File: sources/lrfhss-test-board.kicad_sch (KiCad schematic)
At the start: 9 parts, among them J1 USB-C, U1 LoRa126XF30

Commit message: feat: add initial version of the schematic
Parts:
- added C1, C2: 1uF, footprints:CAP0805, symbol capacitors:C0805C105K5RACTU
- added C3: 47uF, footprints:CAP2917POL, symbol capacitors:T495X476K035ATE300
- added C4: 100nF, footprints:CAP0603, symbol capacitors:C0603C104K5RACTU
- added D1: LED, symbol Device:LED
- added J2, J3: 532610271, footprints:532610271, symbol 532610271:532610271
- added J4: 532610471, footprints:532610471, symbol 532610471:532610471
- added R4: 1k, footprints:RES0603, symbol resistors:CRCW06031K00FKEAHP
- added U2: AMS1117-3.3, Package_TO_SOT_SMD:SOT-223-3_TabPin2, symbol Regulator_Linear:AMS1117-3.3
- J1: footprint (none) -> footprinst:GENERIC-USB-C.step
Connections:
- net GND: now also J1.A1 (GND), J1.B1 (GND), U1.15 (GND), U1.2 (GND), U1.8 (GND), C1.1, C2.1, C3.2, C4.1, D1.1 (K), U2.1 (GND)
- net VBUS: now also J1.A4 (VBUS), J1.B4 (VBUS), U1.1 (VCC), C1.2, C3.1, C4.2, R4.2, U2.3 (VI)
- net SPI1: now reaches U1.10 (MISO)
- net SPI1: now also J4.2
- net SPI0: now reaches U1.11 (MOSI)
- net SPI0: now also J4.1
- net DATA1: now reaches U1.13 (DIO1)
- net DATA1: now also J3.2
- net DATA0: now reaches U1.14 (DIO3)
- net DATA0: now also J3.1
- net ANT: now reaches U1.16 (ANT)
- net CTRL0: now reaches U1.5 (~{RESET})
- net CTRL0: now also J2.1
- net CTRL1: now reaches U1.6 (BUSY)
- net CTRL1: now also J2.2
- net SPI3: now reaches U1.7 (~{NSS})
- net SPI3: now also J4.4
- net SPI2: now reaches U1.9 (SCK)
- net SPI2: now also J4.3
- new net: D1.2 (A), R4.1
- new net 3V3: C2.2, U2.2 (VO)
- no-connect marks 0 -> 6
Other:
- moved on the sheet: R1, R2, R3, U1

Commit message: feat: improve schematic and layout
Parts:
- added J5: 142-0701-801, footprints:142-0701-801, symbol connectors:142-0701-801
- D1: footprint (none) -> LED_SMD:LED_0603_1608Metric
- J1: footprint footprinst:GENERIC-USB-C.step -> footprints:GENERIC-USB-C
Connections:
- net ANT: now also J5.1
- net CTRL0: now also J2.2; no longer J2.1
- net CTRL1: now also J2.1; no longer J2.2
- net GND: now also J5.S1, J5.S2, J5.S3, J5.S4
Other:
- moved on the sheet: C1, C2, C3, C4, D1, J1, J2, J3, J4, R1, R2, R3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

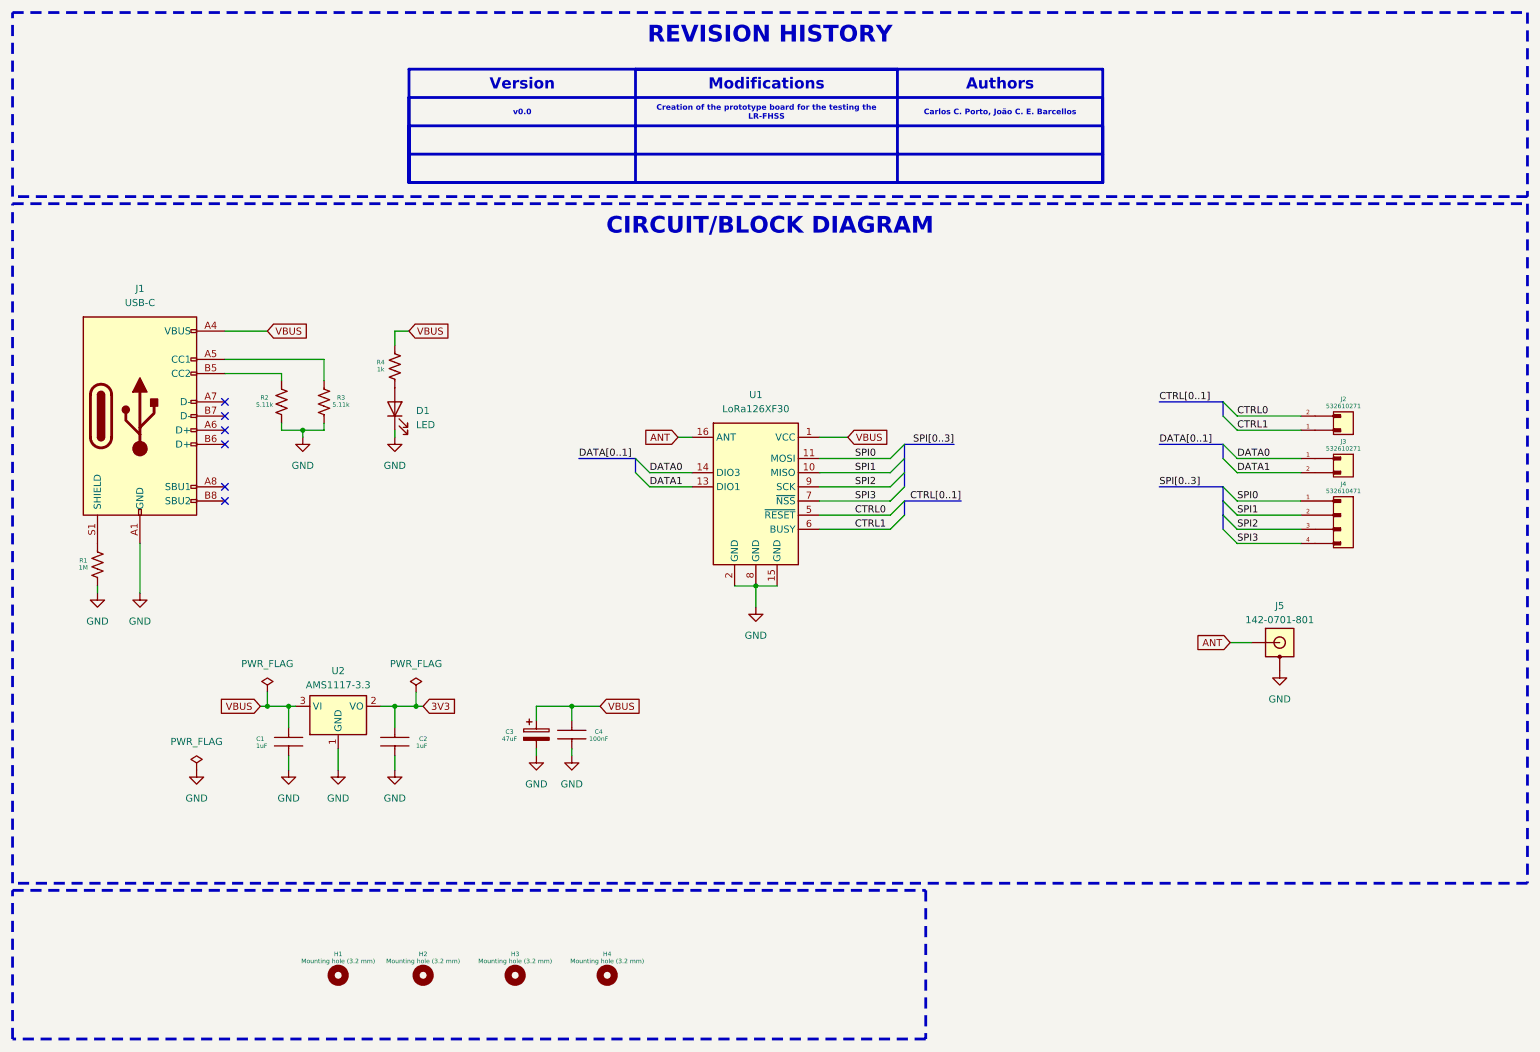
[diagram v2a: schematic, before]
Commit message: fix: add pins to interface with jumpers and some connectors for power
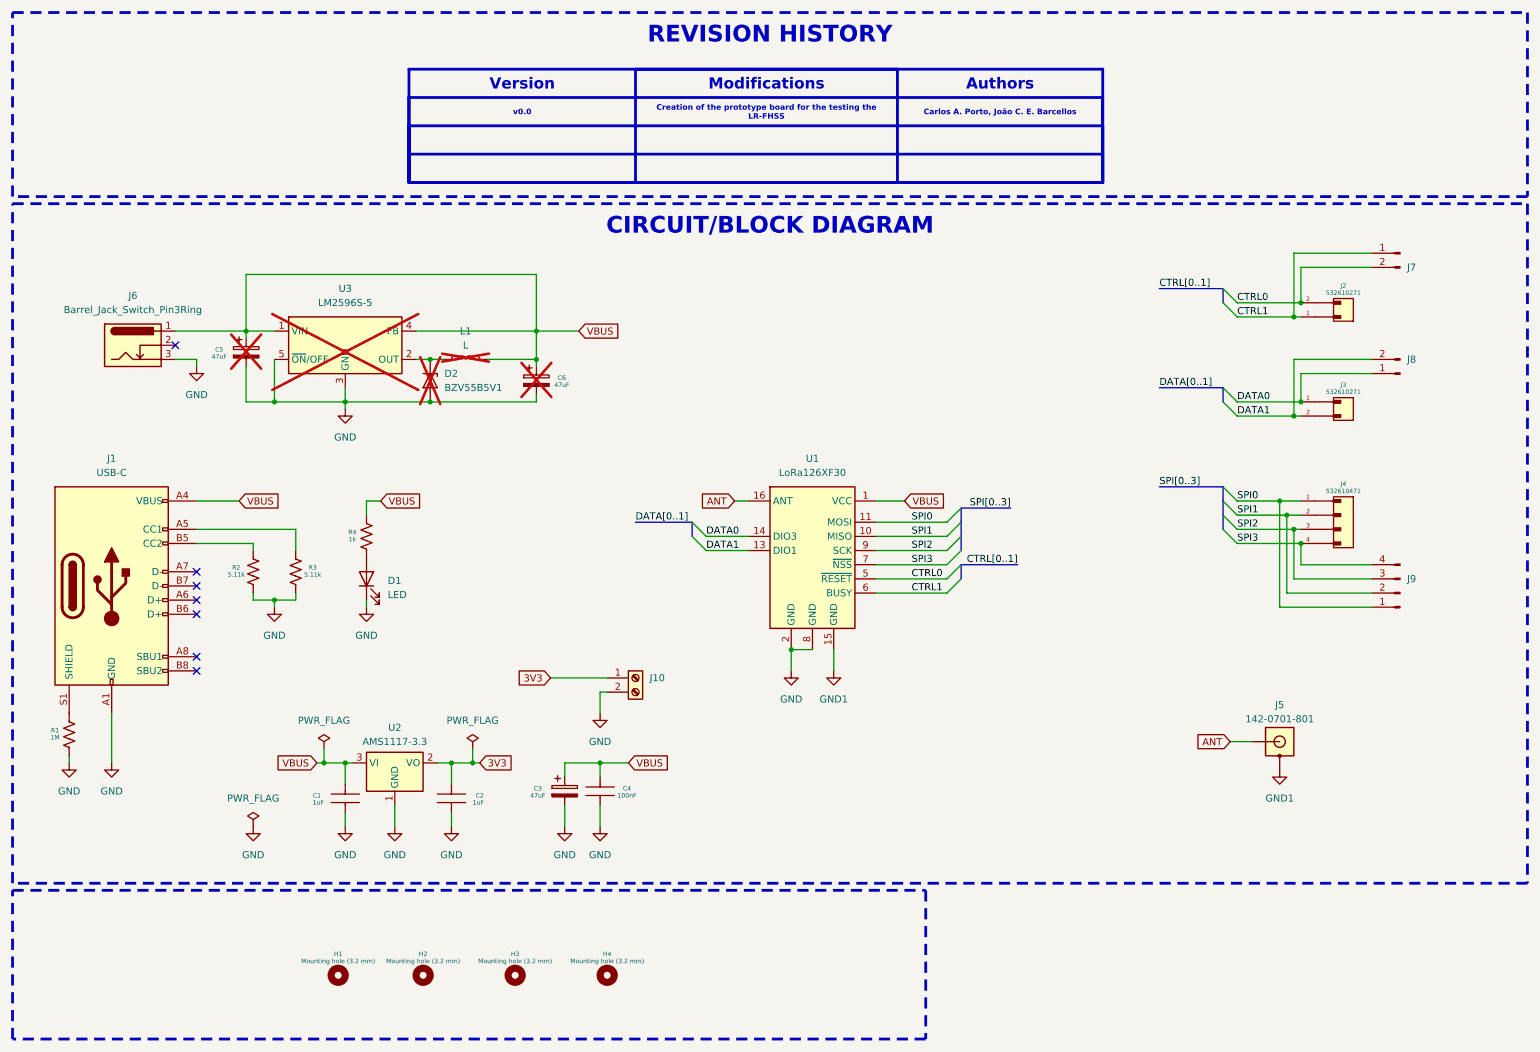
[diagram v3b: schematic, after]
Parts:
- added C5, C6: 47uF, footprints:CAP2917POL, symbol capacitors:T495X476K035ATE300
- added D2: BZV55B5V1, Diode_SMD:D_MiniMELF, symbol Diode:BZV55B5V1
- added J10: Screw_Terminal_01x02, footprints:MV-152, symbol Connector:Screw_Terminal_01x02
- added J6: Barrel_Jack_Switch_Pin3Ring, footprints:DC_Power_Jack_PCB_Mounted_2.1mm, symbol Connector:Barrel_Jack_Switch_Pin3Ring
- added J7, J8: Conn_01x02_Pin, footprints:TSW-102-07-G-S, symbol Connector:Conn_01x02_Pin
- added J9: Conn_01x04_Pin, footprints:TSW-104-07-G-S, symbol Connector:Conn_01x04_Pin
- added L1: L, symbol Device:L
- added U3: LM2596S-5, Package_TO_SOT_SMD:TO-263-5_TabPin3, symbol Regulator_Switching:LM2596S-5
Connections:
- net 3V3: now also J10.1 (Pin_1)
- net CTRL0: now also J7.2 (Pin_2)
- net CTRL1: now also J7.1 (Pin_1)
- net DATA0: now also J8.1 (Pin_1)
- net DATA1: now also J8.2 (Pin_2)
- net GND: now also C5.2, C6.2, D2.2 (A), J10.2 (Pin_2), J6.3, U3.3 (GND), U3.5 (~{ON}/OFF); no longer J5.S1, J5.S2, J5.S3, J5.S4, U1.15 (GND)
- net SPI0: now also J9.1 (Pin_1)
- net SPI1: now also J9.2 (Pin_2)
- net SPI2: now also J9.3 (Pin_3)
- net SPI3: now also J9.4 (Pin_4)
- net VBUS: now also C5.1, C6.1, J6.1, L1.2, U3.1 (VIN), U3.4 (FB)
- new net: D2.1 (K), L1.1, U3.2 (OUT)
- new net GND1: J5.S1, J5.S2, J5.S3, J5.S4, U1.15 (GND)
- no-connect marks 6 -> 7
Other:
- moved on the sheet: C1, C2, C3, C4, D1, J1, J2, J3, J5, R1, R2, R3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

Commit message: fix: add final version to fabricate the board at INEP
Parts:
- removed C3: 47uF, footprints:CAP2917POL, symbol capacitors:T495X476K035ATE300
- added C3: 47uF, footprints:CAP47UELECTROLYTIC, symbol capacitors:ESK476M035AC3AA
- added J11: Screw_Terminal_01x02, footprints:MV-152, symbol Connector:Screw_Terminal_01x02
- J6: now not fitted
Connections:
- net GND: now also C3.2, J11.2 (Pin_2)
- net VBUS: now also C3.1, J11.1 (Pin_1)
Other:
- company: (none) -> Universisdade Federal de Santa Catarina
- moved on the sheet: C1, C2, C4, D1, J1, J10, J2, J3, J4, J5, J7, J8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
